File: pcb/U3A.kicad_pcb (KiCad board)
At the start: 2 copper layers, 34.5 x 26.4 mm, 38 parts, among them J1 Conn_01x03_Pin, J2 Conn_01x07_Pin, J3 USB_C, J4 Conn_01x08_Pin, Q1 AO3401A, SW1 SW_DIP_x02, U1 LD1117S33TR, U2 FT232RL

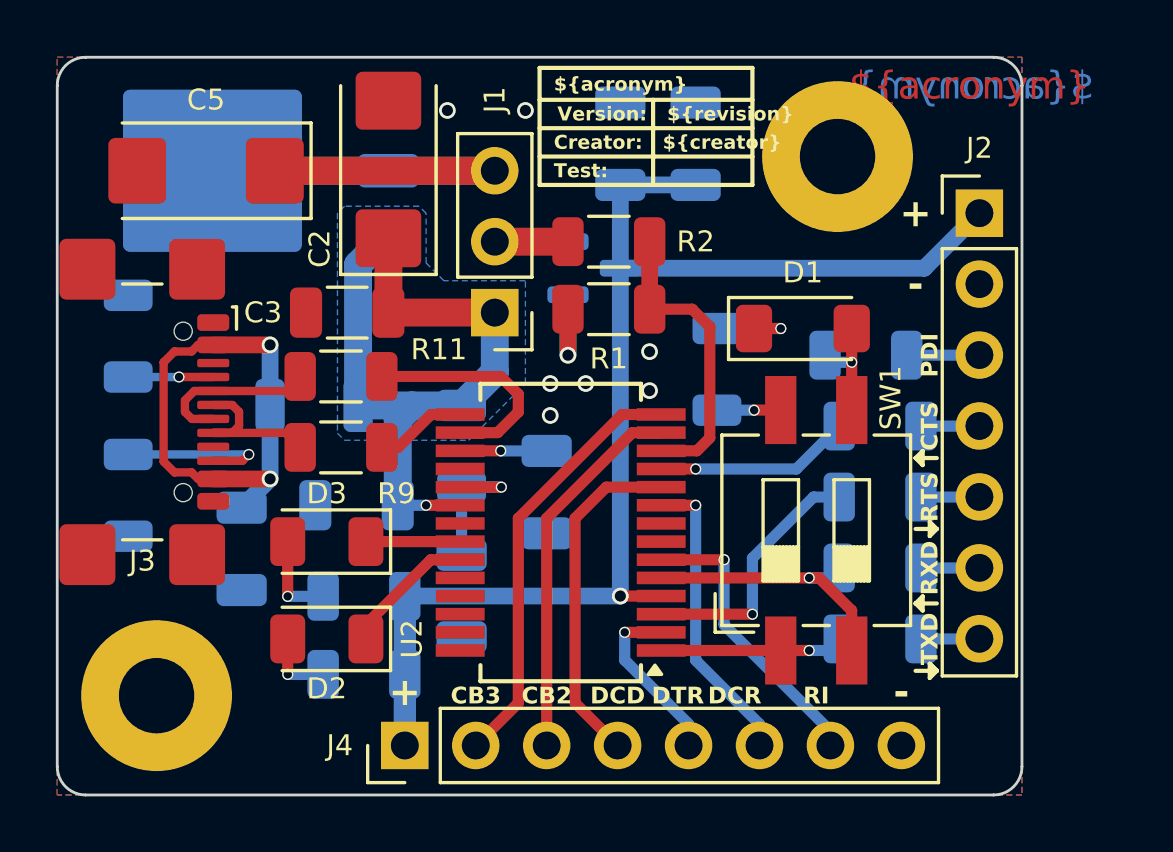
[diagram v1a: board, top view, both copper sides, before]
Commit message: Fix voltage error on startup
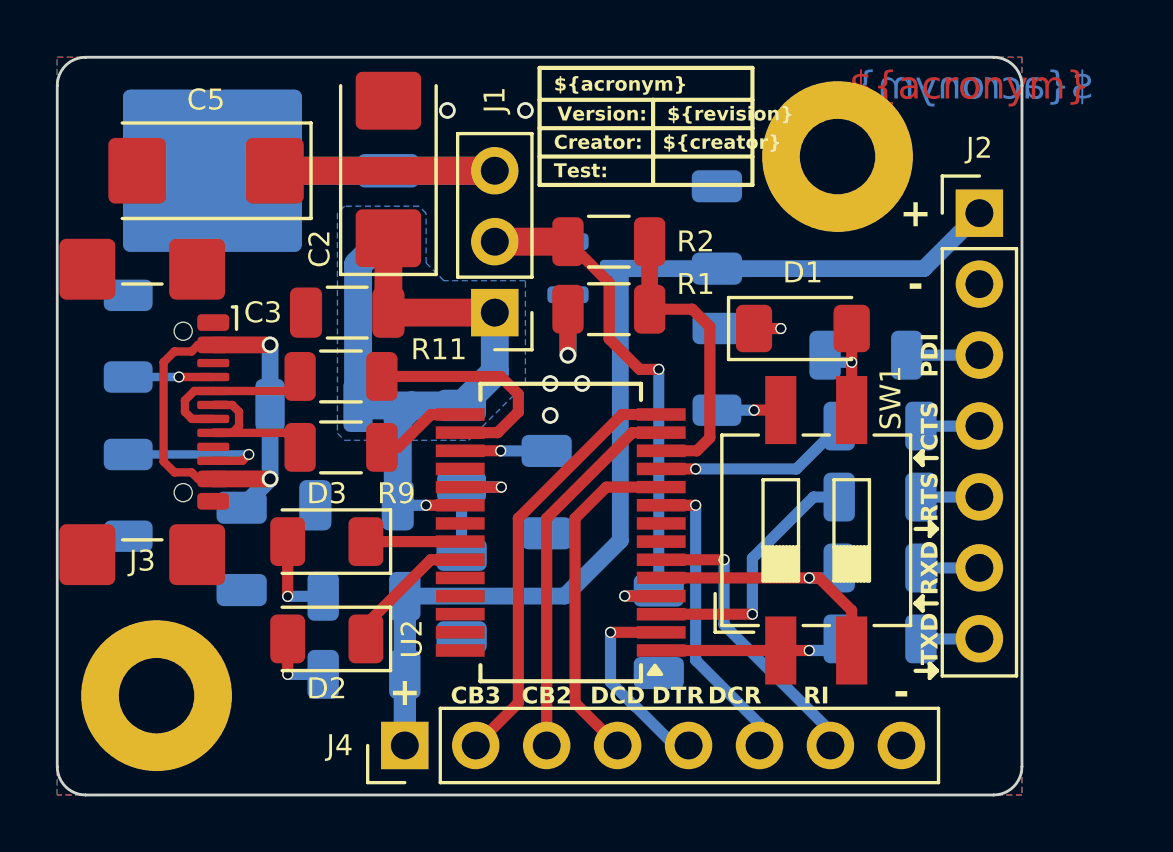
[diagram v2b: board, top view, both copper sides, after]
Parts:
- moved C6 17.5 mm to (166.3, 96.8), turned to 90 degrees
- moved C7 3.09 mm to (168.4, 82.3)
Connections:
- C6 pad 2: VCC -> Net-(J1-Pin_2)
- U2 pad 4: VCC -> Net-(J1-Pin_2)
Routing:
- net Net-(J1-Pin_2): track 5.24 -> 22.1 mm, vias 0 -> 2
- net VCC: track 45.6 -> 37.3 mm, vias 1 -> 0
- net /DTR: track 6.31 -> 7.33 mm
- net GND: vias 7 -> 5
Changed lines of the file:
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@@
       (net 12 "RTS") (pinfunction "RTS") (pintype "output"))
     (pad "4" smd rect (at -3.6 -2.275 180) (size 1.75 0.45) (layers "F.Cu" "F.Paste" "F.Mask")
-      (net 3 "VCC") (pinfunction "VCCIO") (pintype "power_in"))
+      (net 11 "Net-(J1-Pin_2)") (pinfunction "VCCIO") (pintype "power_in"))
     (pad "5" smd rect (at -3.6 -1.625 180) (size 1.75 0.45) (layers "F.Cu" "F.Paste" "F.Mask")
       (net 23 "RXD") (pinfunction "RXD") (pintype "input"))
@@
     (property "ki_keywords" "R res resistor")
     (attr smd)
-    (fp_text reference "R1" (at 0 -1.773382 -360) (layer "F.SilkS")
+    (fp_text reference "R1" (at -3.1095 0.893618 -360) (layer "F.SilkS")
         (effects (font (size 0.75 0.75) (thickness 0.12)))
     )
@@
   )
   (footprint "Capacitor_SMD:C_1206_3216Metric" (layer "B.Cu")
-    (at 167.64 79.297 -90)
+    (at 168.402 82.2942 -90)
     (descr "Capacitor SMD 1206 (3216 Metric), square (rectangular) end terminal, IPC_7351 nominal, (Body size source: IPC-SM-782 page 76, https://www.pcb-3d.com/wordpress/wp-content/uploads/ipc-sm-782a_amendment_1_and_2.pdf), generated with kicad-footprint-generator")
     (tags "capacitor")
@@
   )
   (footprint "Capacitor_SMD:C_1206_3216Metric" (layer "B.Cu")
-    (at 164.943 79.297 -90)
+    (at 166.3192 96.774 90)
     (descr "Capacitor SMD 1206 (3216 Metric), square (rectangular) end terminal, IPC_7351 nominal, (Body size source: IPC-SM-782 page 76, https://www.pcb-3d.com/wordpress/wp-content/uploads/ipc-sm-782a_amendment_1_and_2.pdf), generated with kicad-footprint-generator")
     (tags "capacitor")
@@
     (property "ki_keywords" "cap capacitor")
     (attr smd)
-    (fp_text reference "C6" (at 0 1.494 90) (layer "B.SilkS")
+    (fp_text reference "C6" (at 0.0018 -2.7432 90) (layer "B.SilkS")
         (effects (font (size 0.75 0.75) (thickness 0.12)) (justify mirror))
     )
@@
     (fp_line (start 1.6 0.8) (end 1.6 -0.8)
       (stroke (width 0.1) (type solid)) (layer "B.Fab"))
-    (pad "1" smd roundrect (at -1.475 0 270) (size 1.15 1.8) (layers "B.Cu" "B.Paste" "B.Mask") (roundrect_rratio 0.2173913043)
+    (pad "1" smd roundrect (at -1.475 0 90) (size 1.15 1.8) (layers "B.Cu" "B.Paste" "B.Mask") (roundrect_rratio 0.2173913043)
       (net 1 "GND") (pintype "passive"))
-    (pad "2" smd roundrect (at 1.475 0 270) (size 1.15 1.8) (layers "B.Cu" "B.Paste" "B.Mask") (roundrect_rratio 0.2173913043)
-      (net 3 "VCC") (pintype "passive"))
+    (pad "2" smd roundrect (at 1.475 0 90) (size 1.15 1.8) (layers "B.Cu" "B.Paste" "B.Mask") (roundrect_rratio 0.2173913043)
+      (net 11 "Net-(J1-Pin_2)") (pintype "passive"))
     (model "${KICAD6_3DMODEL_DIR}/Capacitor_SMD.3dshapes/C_1206_3216Metric.wrl"
       (offset (xyz 0 0 0))
@@
     (property "ki_keywords" "R res resistor")
     (attr smd)
-    (fp_text reference "R5" (at 0 1.524 90) (layer "B.SilkS")
+    (fp_text reference "R5" (at 0 -1.778 90) (layer "B.SilkS")
         (effects (font (size 0.75 0.75) (thickness 0.12)) (justify mirror))
     )
@@
   )
   (via (at 162.433 87.884) (size 0.6) (drill 0.4) (layers "F.Cu" "B.Cu") (free) (net 1))
-  (via (at 163.703 87.884) (size 0.6) (drill 0.4) (layers "F.Cu" "B.Cu") (free) (net 1))
-  (via (at 165.989 88.138) (size 0.6) (drill 0.4) (layers "F.Cu" "B.Cu") (free) (net 1))
-  (via (at 165.989 86.741) (size 0.6) (drill 0.4) (layers "F.Cu" "B.Cu") (free) (net 1))
   (via (at 162.433 89.027) (size 0.6) (drill 0.4) (layers "F.Cu" "B.Cu") (free) (net 1))
+  (via (at 163.576 87.884) (size 0.6) (drill 0.4) (layers "F.Cu" "B.Cu") (free) (net 1))
   (via (at 158.75 78.105) (size 0.6) (drill 0.4) (layers "F.Cu" "B.Cu") (free) (net 1))
   (via (at 161.544 78.105) (size 0.6) (drill 0.4) (layers "F.Cu" "B.Cu") (free) (net 1))
@@
   (segment (start 155.55 88.668) (end 155.55 83.631618) (width 1) (layer "B.Cu") (net 2))
   (segment (start 156.972 92.243) (end 156.972 89.176) (width 1) (layer "B.Cu") (net 2))
-  (segment (start 164.943 95.493) (end 166.407618 95.493) (width 0.4) (layer "F.Cu") (net 3))
-  (via (at 164.943 95.493) (size 0.6) (drill 0.4) (layers "F.Cu" "B.Cu") (net 3))
-  (segment (start 157.237 95.493) (end 164.943 95.493) (width 0.6) (layer "B.Cu") (net 3))
-  (segment (start 175.829 83.754) (end 177.8 81.783) (width 0.6) (layer "B.Cu") (net 3))
-  (segment (start 167.64 80.772) (end 164.943 80.772) (width 0.6) (layer "B.Cu") (net 3))
-  (segment (start 164.943 83.754) (end 175.829 83.754) (width 0.6) (layer "B.Cu") (net 3))
+  (segment (start 164.9582 83.7692) (end 175.8138 83.7692) (width 0.6) (layer "B.Cu") (net 3))
+  (segment (start 164.943 83.754) (end 164.9582 83.7692) (width 0.6) (layer "B.Cu") (net 3))
+  (segment (start 164.943 93.502) (end 164.943 83.754) (width 0.6) (layer "B.Cu") (net 3))
   (segment (start 157.226 97.79) (end 157.226 100.843618) (width 0.8) (layer "B.Cu") (net 3))
+  (segment (start 162.952 95.493) (end 164.943 93.502) (width 0.6) (layer "B.Cu") (net 3))
+  (segment (start 175.8138 83.7692) (end 177.8 81.783) (width 0.6) (layer "B.Cu") (net 3))
   (segment (start 157.226 95.504) (end 157.226 97.79) (width 0.8) (layer "B.Cu") (net 3))
-  (segment (start 164.943 80.772) (end 164.943 83.754) (width 0.6) (layer "B.Cu") (net 3))
+  (segment (start 157.237 95.493) (end 162.952 95.493) (width 0.6) (layer "B.Cu") (net 3))
   (segment (start 157.226 95.504) (end 157.237 95.493) (width 0.6) (layer "B.Cu") (net 3))
-  (segment (start 164.943 95.493) (end 164.943 83.754) (width 0.6) (layer "B.Cu") (net 3))
   (segment (start 170.688 85.9135) (end 169.728 85.9135) (width 0.4) (layer "F.Cu") (net 4))
   (via (at 170.688 85.9135) (size 0.4) (drill 0.3) (layers "F.Cu" "B.Cu") (net 4))
@@
   (via (at 153.032 95.504) (size 0.4) (drill 0.3) (layers "F.Cu" "B.Cu") (net 10))
   (segment (start 153.032 95.504) (end 154.301 95.504) (width 0.4) (layer "B.Cu") (net 10))
+  (segment (start 164.5412 86.28315) (end 164.5412 84.2772) (width 0.4) (layer "F.Cu") (net 11))
   (segment (start 160.447618 82.804) (end 163.068 82.804) (width 1) (layer "F.Cu") (net 11))
+  (segment (start 166.407618 95.493) (end 165.1 95.493) (width 0.4) (layer "F.Cu") (net 11))
+  (segment (start 165.63405 87.376) (end 164.5412 86.28315) (width 0.4) (layer "F.Cu") (net 11))
+  (segment (start 164.5412 84.2772) (end 163.068 82.804) (width 0.4) (layer "F.Cu") (net 11))
+  (segment (start 166.3192 87.376) (end 165.63405 87.376) (width 0.4) (layer "F.Cu") (net 11))
+  (via (at 166.3192 87.376) (size 0.4) (drill 0.3) (layers "F.Cu" "B.Cu") (net 11))
+  (via (at 165.1 95.493) (size 0.4) (drill 0.3) (layers "F.Cu" "B.Cu") (net 11))
+  (segment (start 166.3192 87.376) (end 166.3192 95.3498) (width 0.4) (layer "B.Cu") (net 11))
+  (segment (start 166.3192 95.3498) (end 166.176 95.493) (width 0.4) (layer "B.Cu") (net 11))
   (segment (start 163.068 82.804) (end 160.447618 82.804) (width 0.6) (layer "B.Cu") (net 11))
+  (segment (start 166.176 95.493) (end 165.1 95.493) (width 0.4) (layer "B.Cu") (net 11))
   (segment (start 166.407618 96.143) (end 169.672 96.143) (width 0.4) (layer "F.Cu") (net 12))
   (via (at 169.672 96.143) (size 0.4) (drill 0.3) (layers "F.Cu" "B.Cu") (net 12))
@@
   (segment (start 171.2465 90.943) (end 172.7815 89.408) (width 0.4) (layer "B.Cu") (net 13))
   (segment (start 167.64 90.943) (end 171.2465 90.943) (width 0.4) (layer "B.Cu") (net 13))
-  (segment (start 166.407618 96.793) (end 165.1 96.793) (width 0.4) (layer "F.Cu") (net 14))
-  (via (at 165.1 96.793) (size 0.4) (drill 0.3) (layers "F.Cu" "B.Cu") (net 14))
-  (segment (start 165.1 97.79) (end 167.386 100.076) (width 0.4) (layer "B.Cu") (net 14))
-  (segment (start 165.1 96.793) (end 165.1 97.79) (width 0.4) (layer "B.Cu") (net 14))
-  (segment (start 167.386 100.076) (end 167.386 100.843618) (width 0.4) (layer "B.Cu") (net 14))
+  (segment (start 166.407618 96.793) (end 164.592 96.793) (width 0.4) (layer "F.Cu") (net 14))
+  (via (at 164.592 96.793) (size 0.4) (drill 0.3) (layers "F.Cu" "B.Cu") (net 14))
+  (segment (start 165.469 99.429) (end 166.883618 100.843618) (width 0.4) (layer "B.Cu") (net 14))
+  (segment (start 164.592 96.793) (end 164.592 98.577166) (width 0.4) (layer "B.Cu") (net 14))
+  (segment (start 165.443834 99.429) (end 165.469 99.429) (width 0.4) (layer "B.Cu") (net 14))
+  (segment (start 166.883618 100.843618) (end 167.386 100.843618) (width 0.4) (layer "B.Cu") (net 14))
+  (segment (start 164.592 98.577166) (end 165.443834 99.429) (width 0.4) (layer "B.Cu") (net 14))
   (segment (start 166.407618 92.243) (end 167.64 92.243) (width 0.4) (layer "F.Cu") (net 15))
   (via (at 167.64 92.243) (size 0.4) (drill 0.3) (layers "F.Cu" "B.Cu") (net 15))
